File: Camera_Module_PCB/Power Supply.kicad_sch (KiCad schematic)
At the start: 4 parts, among them J4 SS-52400-002, U3 LM1117MPX-33NOPB

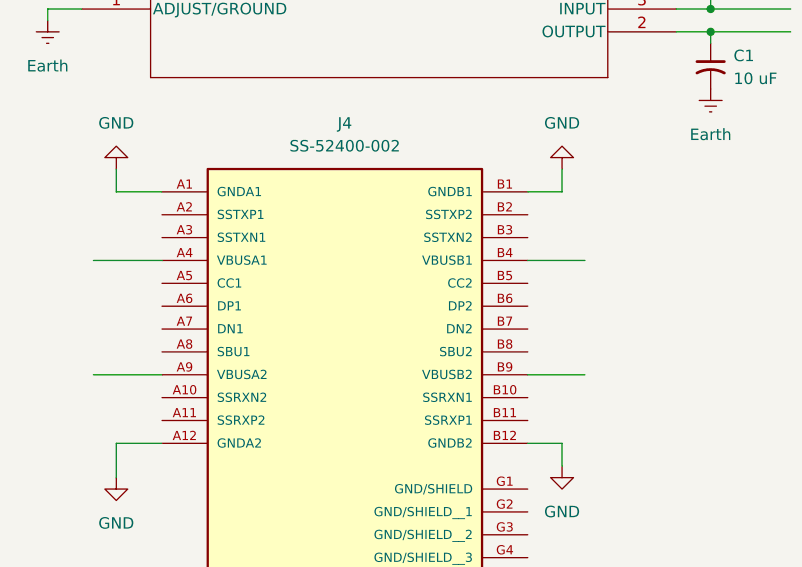
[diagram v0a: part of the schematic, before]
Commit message: Fixed an Error with added sheet name
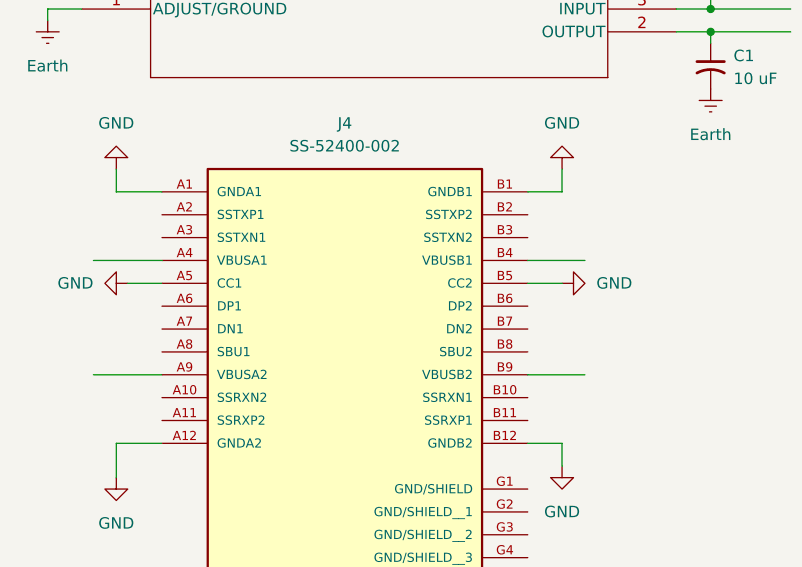
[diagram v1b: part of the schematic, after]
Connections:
- net GND: now also J4.A5 (CC1), J4.B5 (CC2)
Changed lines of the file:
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@@
+	(wire
+		(pts
+			(xy 73.66 80.01) (xy 77.47 80.01)
+		)
+		(stroke
+			(width 0)
+			(type default)
+		)
+	)
 	(wire
 		(pts
@@
 		(pts
 			(xy 68.58 49.53) (xy 64.77 49.53)
+		)
+		(stroke
+			(width 0)
+			(type default)
+		)
+	)
+	(wire
+		(pts
+			(xy 118.11 80.01) (xy 121.92 80.01)
 		)
 		(stroke
@@
 	(symbol
 		(lib_id "power:GND")
+		(at 121.92 80.01 90)
+		(unit 1)
+		(exclude_from_sim no)
+		(in_bom yes)
+		(on_board yes)
+		(dnp no)
+		(fields_autoplaced yes)
+		(property "Reference" "#PWR09"
+			(at 128.27 80.01 0)
+			(effects
+				(font
+					(size 1.27 1.27)
+				)
+				(hide yes)
+			)
+		)
+		(property "Value" "GND"
+			(at 125.73 80.0099 90)
+			(effects
+				(font
+					(size 1.27 1.27)
+				)
+				(justify right)
+			)
+		)
+		(property "Footprint" ""
+			(at 121.92 80.01 0)
+			(effects
+				(font
+					(size 1.27 1.27)
+				)
+				(hide yes)
+			)
+		)
+		(property "Datasheet" ""
+			(at 121.92 80.01 0)
+			(effects
+				(font
+					(size 1.27 1.27)
+				)
+				(hide yes)
+			)
+		)
+		(property "Description" "Power symbol creates a global label with name \"GND\" , ground"
+			(at 121.92 80.01 0)
+			(effects
+				(font
+					(size 1.27 1.27)
+				)
+				(hide yes)
+			)
+		)
+		(pin "1"
+		)
+		(instances
+			(project "Camera_Module_PCB"
+				(path "/e3d5a9d6-7dc8-43b3-bd64-189ae9cbab33/097e721d-c536-4567-9b5e-193861a3bee4"
+					(reference "#PWR09")
+					(unit 1)
+				)
+			)
+		)
+	)
+	(symbol
+		(lib_id "power:GND")
 		(at 72.39 67.31 180)
 		(unit 1)
@@
 					(unit 1)
 				)
+			)
+		)
+	)
+	(symbol
+		(lib_id "power:GND")
+		(at 73.66 80.01 270)
+		(unit 1)
+		(exclude_from_sim no)
+		(in_bom yes)
+		(on_board yes)
+		(dnp no)
+		(fields_autoplaced yes)
+		(property "Reference" "#PWR08"
+			(at 67.31 80.01 0)
+			(effects
+				(font
+					(size 1.27 1.27)
+				)
+				(hide yes)
+			)
+		)
+		(property "Value" "GND"
+			(at 69.85 80.0099 90)
+			(effects
+				(font
+					(size 1.27 1.27)
+				)
+				(justify right)
+			)
+		)
+		(property "Footprint" ""
+			(at 73.66 80.01 0)
+			(effects
+				(font
+					(size 1.27 1.27)
+				)
+				(hide yes)
+			)
+		)
+		(property "Datasheet" ""
+			(at 73.66 80.01 0)
+			(effects
+				(font
+					(size 1.27 1.27)
+				)
+				(hide yes)
+			)
+		)
+		(property "Description" "Power symbol creates a global label with name \"GND\" , ground"
+			(at 73.66 80.01 0)
+			(effects
+				(font
+					(size 1.27 1.27)
+				)
+				(hide yes)
+			)
+		)
+		(pin "1"
+		)
+		(instances
+			(project "Camera_Module_PCB"
+				(path "/e3d5a9d6-7dc8-43b3-bd64-189ae9cbab33/097e721d-c536-4567-9b5e-193861a3bee4"
+					(reference "#PWR08")
+					(unit 1)
+				)

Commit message: Updated some elements of the schematic
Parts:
- added C3, C4: 0.1uF, symbol Device:C_Polarized
- added R1, R2: 5.1k, symbol Device:R_US
- added U2: MCP73871T-4CCI/ML, QFN20_4x4MC_MCH, symbol MCP73871T_4CCI_ML:MCP73871T-4CCI_ML
- C1, C2: symbol Device:C_Small_US -> Device:C_Small
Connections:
- net Earth is gone; now on net GND: C1.2, C2.2, U3.1 (ADJUST/GROUND)
- net GND: now also J4.G1 (GND/SHIELD), C3.2, C4.2, R1.1, R2.2; no longer J4.A5 (CC1), J4.B5 (CC2)
- net +3.3V: now reaches C1.1, U3.2 (OUTPUT)
- net +3.3V: now also C4.1
- net +5V: now reaches C2.1, U3.3 (INPUT)
- net +5V: now also C3.1
- new net: J4.A5 (CC1), R1.2
- new net: J4.B5 (CC2), R2.1
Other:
- moved on the sheet: C1, C2, J4, U3

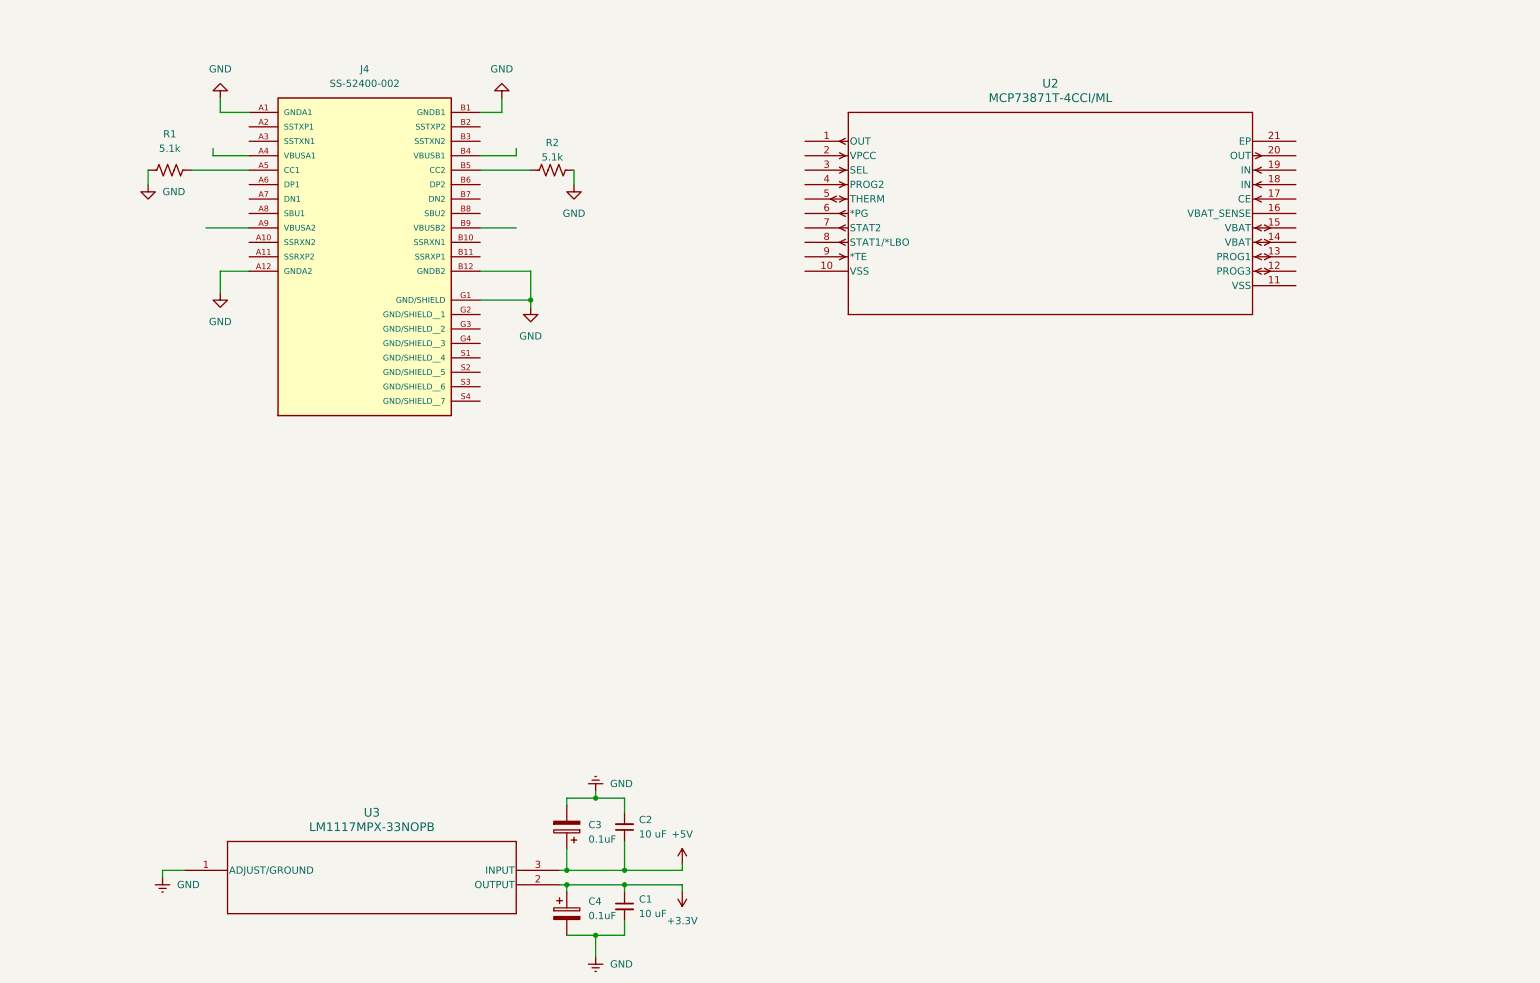
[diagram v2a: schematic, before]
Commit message: Modified the power supply and organized folders
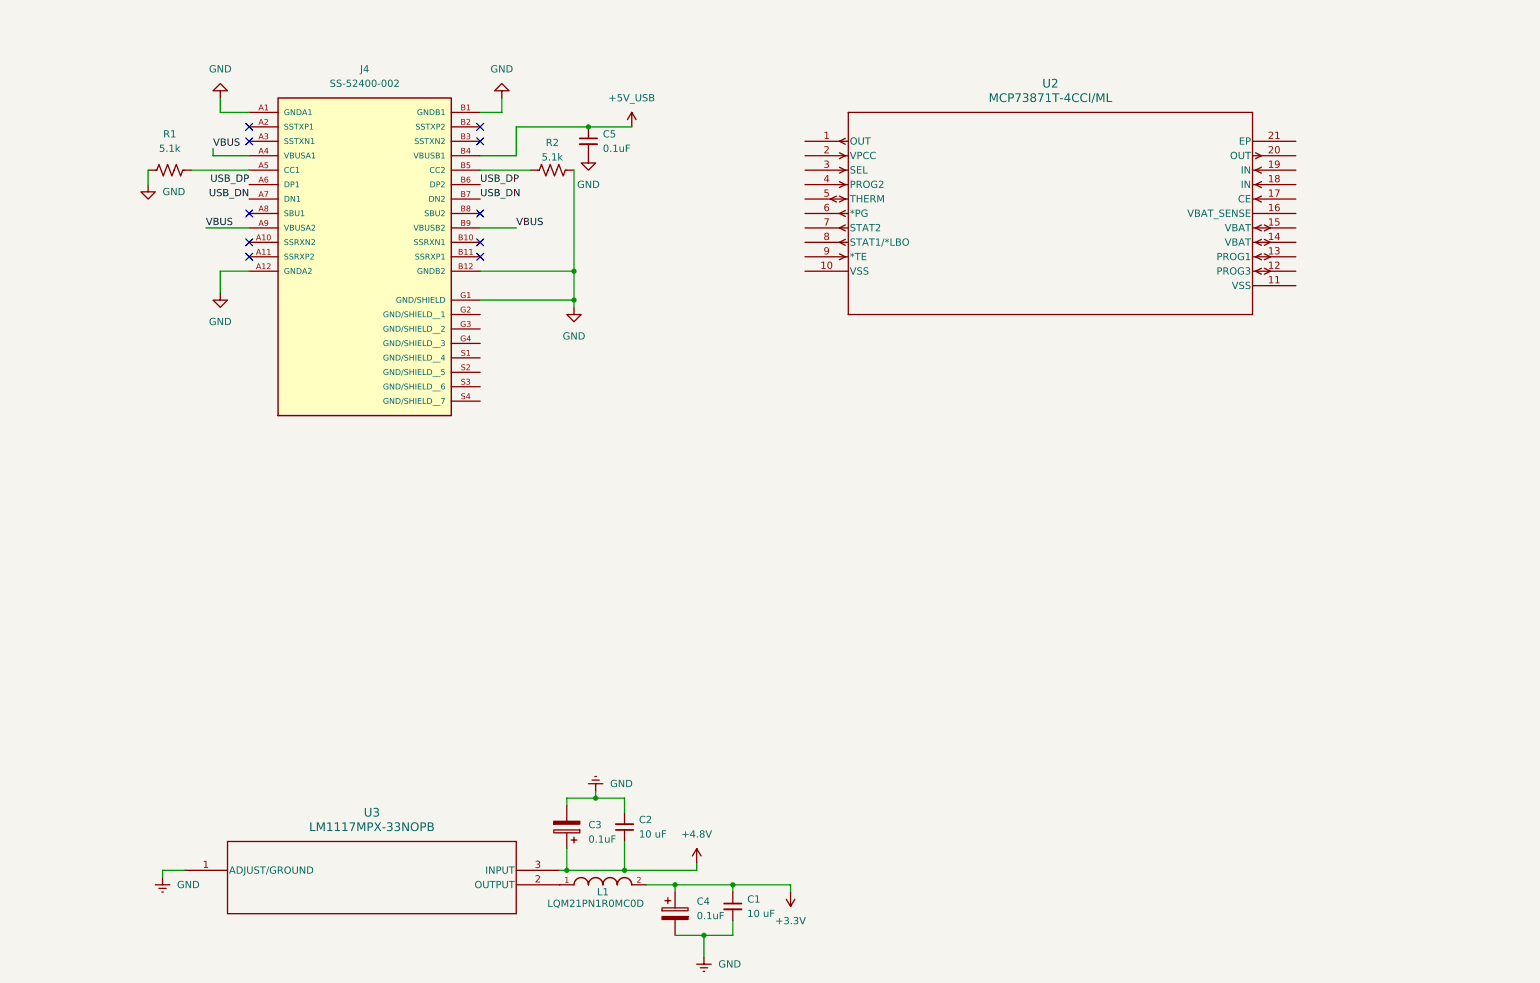
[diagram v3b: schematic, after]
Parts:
- added C5: 0.1uF, symbol Device:C_Small
- added L1: LQM21PN1R0MC0D, LQM21PN1R0MC0D:INDC2012X55N, symbol LMQ21PN1R0:LQM21PN1R0MC0D
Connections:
- net +3.3V: now also L1.2; no longer U3.2 (OUTPUT)
- net GND: now also C5.2
- net VBUS: now reaches J4.A4 (VBUSA1)
- net VBUS: now also J4.A9 (VBUSA2), J4.B9 (VBUSB2)
- net USB_DP: now reaches J4.A6 (DP1)
- net USB_DP: now also J4.B6 (DP2)
- net USB_DN: now reaches J4.A7 (DN1)
- net USB_DN: now also J4.B7 (DN2)
- net +5V_USB: now reaches J4.B4 (VBUSB1)
- net +5V_USB: now also C5.1
- net +5V renamed +4.8V
- new net: L1.1, U3.2 (OUTPUT)
- no-connect marks 0 -> 10
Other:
- moved on the sheet: C1, C4

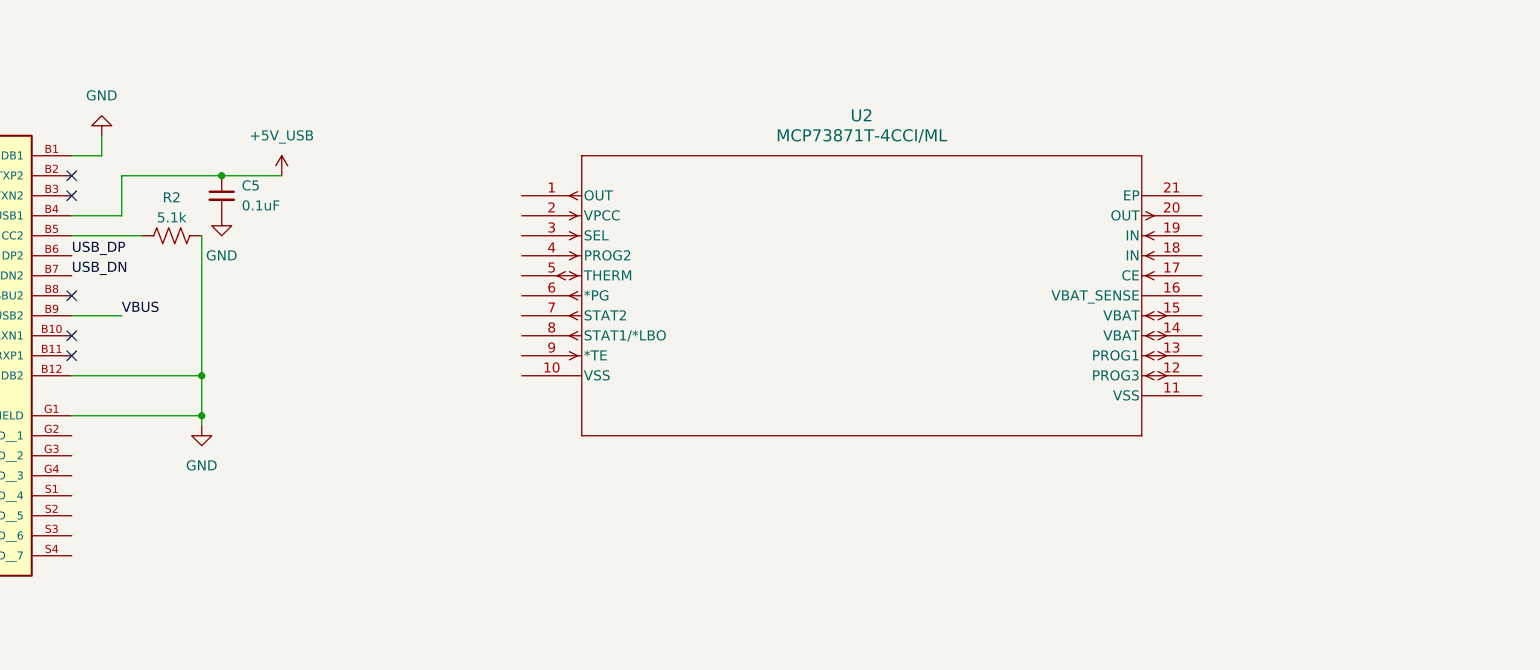
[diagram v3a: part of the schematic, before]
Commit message: Made some new connections on the charging module
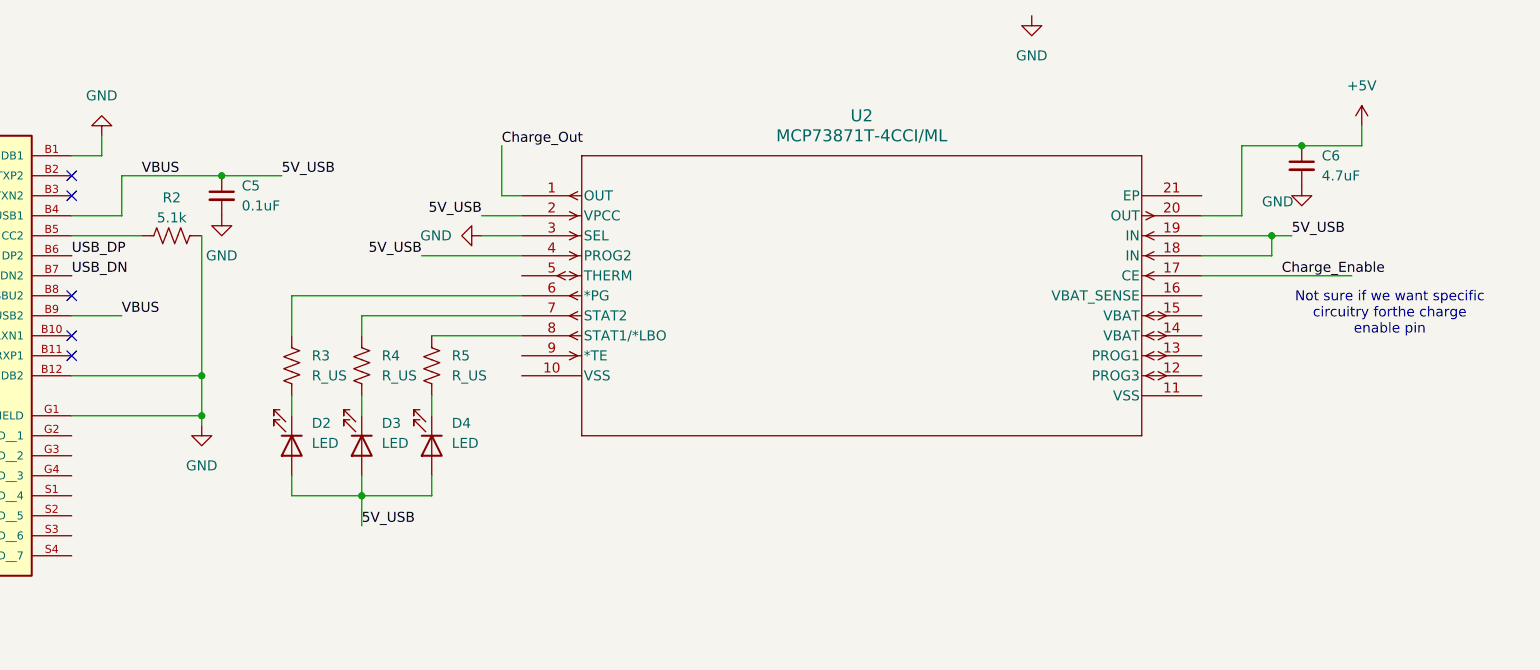
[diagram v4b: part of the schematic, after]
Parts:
- added C6: 4.7uF, symbol Device:C_Small
- added D2, D3, D4: LED, symbol Device:LED
- added R3, R4, R5: R_US, symbol Device:R_US
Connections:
- net +5V_USB is gone; now on net 5V_USB: C5.1, J4.B4 (VBUSB1)
- net VBUS is gone; now on net 5V_USB: J4.A4 (VBUSA1), J4.A9 (VBUSA2), J4.B9 (VBUSB2)
- net GND: now also U2.3 (SEL), C6.2
- net Charge_Out: now reaches U2.1 (OUT)
- net Charge_Enable: now reaches U2.17 (CE)
- net 5V_USB: now reaches U2.18 (IN)
- net 5V_USB: now also U2.19 (IN), U2.2 (VPCC), U2.4 (PROG2), D2.2 (A), D3.2 (A), D4.2 (A)
- net +5V: now reaches U2.20 (OUT)
- net +5V: now also C6.1
- net at U2.6 (*PG): now also R3.1
- net at U2.7 (STAT2): now also R4.1
- net at U2.8 (STAT1/*LBO): now also R5.1
- new net: D4.1 (K), R5.2
- new net: D2.1 (K), R3.2
- new net: D3.1 (K), R4.2
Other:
- note added: "Not sure if we want specific circuitry forthe charge enable pin"

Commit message: Quick Refresh
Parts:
- renumbered C5 to C1, C6 to C?, C1 to C?, C4 to C?, C3 to C?, C2 to C?, D4 to D?, D2 to D?, D3 to D?, L1 to L?, U2 to PMIC, R3 to R?, R4 to R?, R5 to R?, J4 to TypeCinput, U3 to U?
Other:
- note added: "Battery Charge Management Controller"
- note added: "CC Pins are connected to ground since its a Power Sink(it needs power)"
- note added: "Changes from battery to USB C automatically when plugged in"
- note added: "Type C Connector"
- moved on the sheet: C1, C?, D?, PMIC, R1, R2, R?, TypeCinput
